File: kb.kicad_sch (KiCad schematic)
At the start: 7 parts, among them J1 USB_C_Receptacle_USB2.0_16P, U1 nRF52840, U2 MIC23051-CGYML

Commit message: more schematics work
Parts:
- added C4: 1u, symbol Device:C
- added C5, C6: 10p, symbol Device:C
- added C7: 0p8, symbol Device:C
- added C8: 0p5, symbol Device:C
- added L2: 4n7, symbol Device:L
- added U3: BQ25185DLHR, Package_SON:WSON-8-1EP_2x2mm_P0.5mm_EP0.9x1.6mm, symbol Battery_Management_Extra:BQ25185DLHR
- added Y1: XRCGB32M000F1S1CR0, symbol Device:Crystal_GND24
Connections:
- net +BATT: no longer C1.1, U2.2 (EN), U2.3 (VSC), U2.7 (VIN)
- net GND: now also U1.B7 (VSS), U1.EP (VSS), U1.F23 (VSS_PA), C4.1, C5.2, C6.2, C7.2, C8.2, U3.5 (GND), U3.9 (STAT1), Y1.2, Y1.4
- net VBUS: now also C4.2, U3.10 (IN)
- net USB_DP: now reaches J1.A6 (D+), J1.B6 (D+)
- net USB_DN: now reaches J1.A7 (D-), J1.B7 (D-)
- net at U1.H23 (ANT): now also C7.1, L2.2
- new net: C1.1, U2.2 (EN), U2.3 (VSC), U2.7 (VIN)
- new net: C8.1, L2.1
- new net XIN: C6.1, Y1.1
- new net XOUT: C5.1, Y1.3
- no-connect marks 3 -> 4
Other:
- note added: "Note: Buy 12p caps for testing"
- moved on the sheet: U1

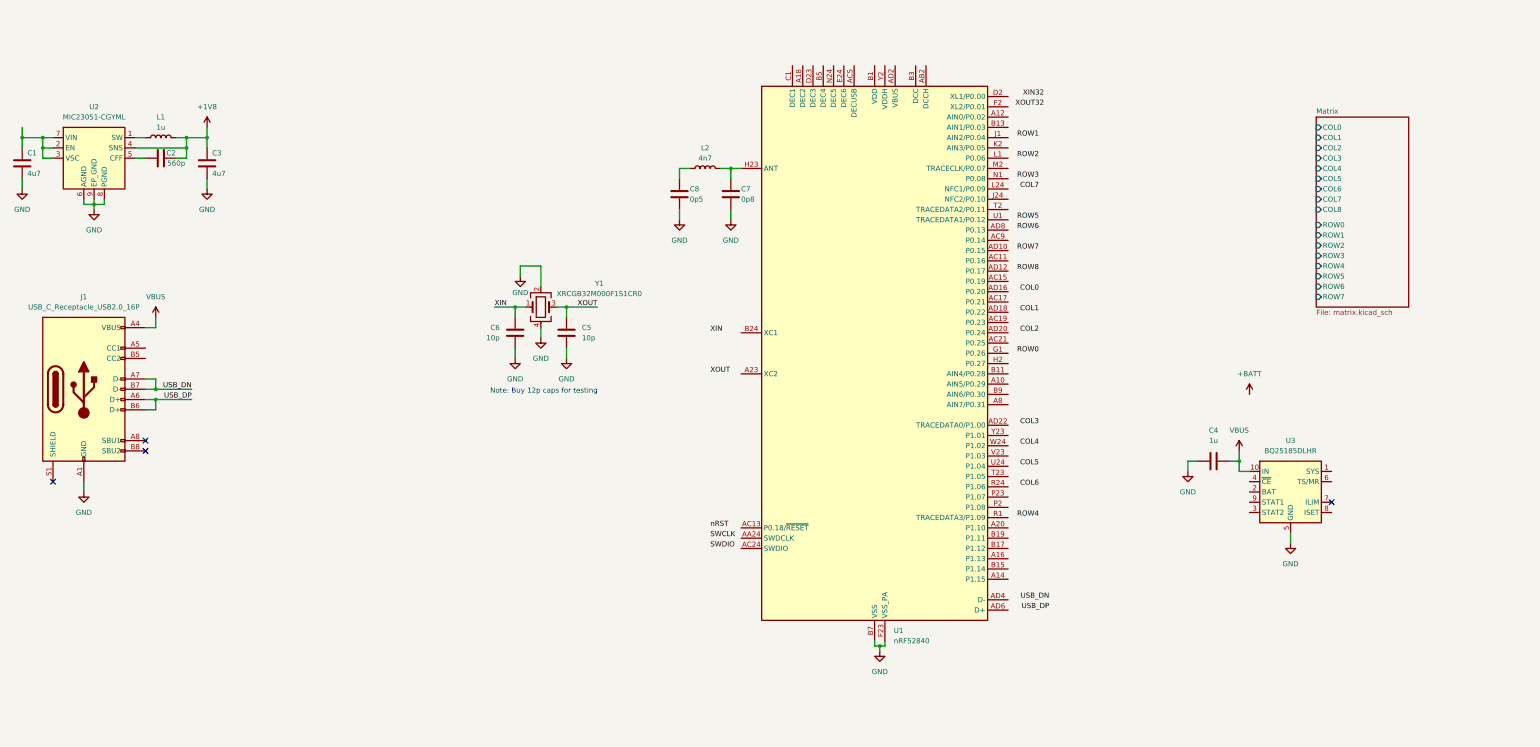
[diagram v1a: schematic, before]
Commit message: update layout and switch to wired
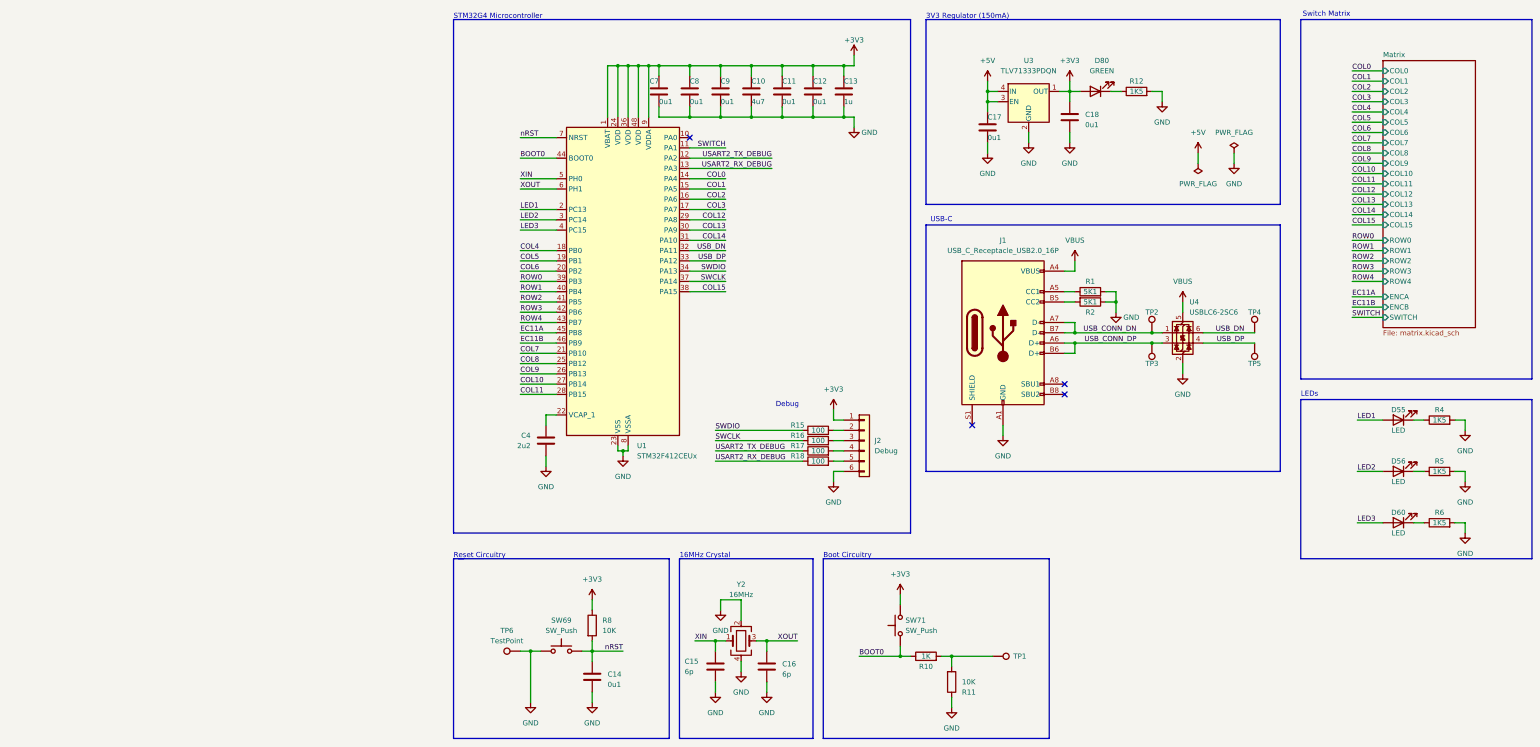
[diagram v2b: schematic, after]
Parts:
- removed C1, C3: 4u7, symbol Device:C
- removed C2: 560p, symbol Device:C
- removed C5, C6: 10p, symbol Device:C
- removed L1: 1u, symbol Device:L
- removed L2: 4n7, symbol Device:L
- removed U1: nRF52840, Package_DFN_QFN:Nordic_AQFN-73-1EP_7x7mm_P0.5mm, symbol MCU_Nordic:nRF52840
- removed U2: MIC23051-CGYML, Package_DFN_QFN:Micrel_MLF-8-1EP_2x2mm_P0.5mm_EP0.6x1.2mm_ThermalVias, symbol Regulator_Switching_Extra:MIC23051-CGYML
- removed U3: BQ25185DLHR, Package_SON:WSON-8-1EP_2x2mm_P0.5mm_EP0.9x1.6mm, symbol Battery_Management_Extra:BQ25185DLHR
- removed Y1: XRCGB32M000F1S1CR0, symbol Device:Crystal_GND24
- added C10: 4u7, Capacitor_SMD:C_0201_0603Metric, symbol Device:C
- added C11, C12, C14, C9: 0u1, Capacitor_SMD:C_0201_0603Metric, symbol Device:C
- added C13: 1u, Capacitor_SMD:C_0201_0603Metric, symbol Device:C
- added C15, C16: 6p, Capacitor_SMD:C_0402_1005Metric, symbol Device:C
- added C17, C18: 0u1, Capacitor_SMD:C_0603_1608Metric, symbol Device:C
- added D55, D56, D60: LED, symbol Device:LED
- added D80: GREEN, LED_SMD:LED_0402_1005Metric, symbol Device:LED
- added J2: Debug, symbol Connector_Generic:Conn_01x06
- added R1, R2: 5K1, symbol Device:R
- added R10: 1K, Resistor_SMD:R_0201_0603Metric, symbol Device:R
- added R11: 10K, Resistor_SMD:R_0402_1005Metric, symbol Device:R
- added R12: 1K5, Resistor_SMD:R_0402_1005Metric, symbol Device:R
- added R15, R16, R17, R18: 100, symbol Device:R
- added R4, R5, R6: 1K5, symbol Device:R
- added R8: 10K, Resistor_SMD:R_0201_0603Metric, symbol Device:R
- added SW69, SW71: SW_Push, symbol Switch:SW_Push
- added TP1: TestPoint, TestPoint:TestPoint_Pad_1.0x1.0mm, symbol Connector:TestPoint
- added TP2, TP3, TP4, TP5, TP6: TestPoint, symbol Connector:TestPoint
- added U1: STM32F412CEUx, Package_DFN_QFN:QFN-48-1EP_7x7mm_P0.5mm_EP5.6x5.6mm, symbol MCU_ST_STM32F4:STM32F412CEUx
- added U3: TLV71333PDQN, Package_SON:Texas_X2SON-4_1x1mm_P0.65mm, symbol TLV71333PDQ:TLV71333PDQN
- added U4: USBLC6-2SC6, Package_TO_SOT_SMD:SOT-23-6, symbol Power_Protection:USBLC6-2SC6
- added Y2: 16MHz, Crystal:Crystal_SMD_2016-4Pin_2.0x1.6mm, symbol Device:Crystal_GND24
- C4: value 1u -> 2u2
- C7: value 0p8 -> 0u1; footprint (none) -> Capacitor_SMD:C_0201_0603Metric; LCSC (none) -> C907967
- C8: value 0p5 -> 0u1; footprint (none) -> Capacitor_SMD:C_0201_0603Metric; LCSC (none) -> C907967
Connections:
- net COL0: now also U1.14 (PA4)
- net COL1: now also U1.15 (PA5)
- net COL2: now also U1.16 (PA6)
- net COL3: now also U1.17 (PA7)
- net COL4: now also U1.18 (PB0)
- net COL5: now also U1.19 (PB1)
- net COL6: now also U1.20 (PB2)
- net COL7: now also U1.21 (PB10)
- net GND: now also C4.2, C10.2, C11.2, C12.2, C13.2, C14.2, C15.2, C16.2, C17.2, C18.2, C9.2, J2.6 (Pin_6), R1.2, R11.1, R12.2, R2.1, R4.2, R5.2, R6.2, SW69.1, TP6.1, U1.23 (VSS), U1.35 (VSS), U1.47 (VSS), U1.49 (VSS), U1.8 (VSSA), U3.2 (GND), U3.5 (GND), U4.2 (GND), Y2.2, Y2.4; no longer C4.1
- net ROW0: now also U1.39 (PB3)
- net ROW1: now also U1.40 (PB4)
- net ROW2: now also U1.41 (PB5)
- net ROW3: now also U1.42 (PB6)
- net ROW4: now also U1.43 (PB7)
- net SWCLK: now also R16.1, U1.37 (PA14)
- net SWDIO: now also R15.1, U1.34 (PA13)
- net USB_DN: now also TP4.1, U1.32 (PA11), U4.6 (I/O1); no longer J1.A7 (D-), J1.B7 (D-)
- net USB_DP: now also TP5.1, U1.33 (PA12), U4.4 (I/O2); no longer J1.A6 (D+), J1.B6 (D+)
- net VBUS: now also U4.5 (VBUS); no longer C4.2
- net XIN: now also C15.1, U1.5 (PH0), Y2.1
- net XOUT: now also C16.1, U1.6 (PH1), Y2.3
- net nRST: now also C14.1, R8.2, SW69.2, U1.7 (NRST)
- net at J1.A5 (CC1): now also R1.1
- net at J1.B5 (CC2): now also R2.2
- net +3V3: now reaches C8.1
- net +3V3: now also C7.1, C10.1, C11.1, C12.1, C13.1, C18.1, C9.1, D80.2 (A), J2.1 (Pin_1), R8.1, SW71.2, U1.1 (VBAT), U1.24 (VDD), U1.36 (VDD), U1.48 (VDD), U1.9 (VDDA), U3.1 (OUT)
- new net: D60.1 (K), R6.1
- new net: D56.1 (K), R5.1
- new net: J2.5 (Pin_5), R18.2
- new net: J2.4 (Pin_4), R17.2
- new net: C4.1, U1.22 (VCAP_1)
- new net: D55.1 (K), R4.1
- new net: R10.2, R11.2, TP1.1
- new net: J2.3 (Pin_3), R16.2
- new net: D80.1 (K), R12.1
- new net: J2.2 (Pin_2), R15.2
- new net +5V: C17.1, U3.3 (EN), U3.4 (IN)
- new net BOOT0: R10.1, SW71.1, U1.44 (BOOT0)
- new net COL10: U1.27 (PB14)
- new net COL11: U1.28 (PB15)
- new net COL12: U1.29 (PA8)
- new net COL13: U1.30 (PA9)
- new net COL14: U1.31 (PA10)
- new net COL15: U1.38 (PA15)
- new net COL8: U1.25 (PB12)
- new net COL9: U1.26 (PB13)
- new net EC11A: U1.45 (PB8)
- new net EC11B: U1.46 (PB9)
- new net LED1: D55.2 (A), U1.2 (PC13)
- new net LED2: D56.2 (A), U1.3 (PC14)
- new net LED3: D60.2 (A), U1.4 (PC15)
- new net SWITCH: U1.11 (PA1)
- new net USART2_RX_DEBUG: R18.1, U1.13 (PA3)
- new net USART2_TX_DEBUG: R17.1, U1.12 (PA2)
- new net USB_CONN_DN: J1.A7 (D-), J1.B7 (D-), TP2.1, U4.1 (I/O1)
- new net USB_CONN_DP: J1.A6 (D+), J1.B6 (D+), TP3.1, U4.3 (I/O2)
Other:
- sheet Matrix ports: added COL10, COL11, COL12, COL13, COL14, COL15, COL9, ENCA, ENCB, SWITCH; removed ROW5, ROW6, ROW7
- note added: "16MHz Crystal"
- note added: "3V3 Regulator (150mA)"
- note added: "Boot Circuitry"
- note added: "Debug"
- note added: "LEDs"
- note added: "Reset Circuitry"
- note added: "STM32G4 Microcontroller"
- note added: "Switch Matrix"
- note added: "USB-C"
- note removed: "Note: Buy 12p caps for testing"
- moved on the sheet: J1

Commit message: work on layout and routing
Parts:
- removed J1: USB_C_Receptacle_USB2.0_16P, symbol Connector:USB_C_Receptacle_USB2.0_16P
- removed R1, R2: 5K1, symbol Device:R
- removed TP2, TP3, TP4, TP5: TestPoint, symbol Connector:TestPoint
- removed U4: USBLC6-2SC6, Package_TO_SOT_SMD:SOT-23-6, symbol Power_Protection:USBLC6-2SC6
- added J2: 78171-0004, Connector_Molex:Molex_Pico-EZmate_78171-0004_1x04-1MP_P1.20mm_Vertical, symbol Connector_Generic_MountingPin:Conn_01x04_MountingPin
- C1: renamed from C7; footprint Capacitor_SMD:C_0201_0603Metric -> Capacitor_SMD:C_0402_1005Metric
- C10: renamed from C4; footprint (none) -> Capacitor_SMD:C_0402_1005Metric
- C13: renamed from C14; footprint Capacitor_SMD:C_0201_0603Metric -> Capacitor_SMD:C_0402_1005Metric
- C2: renamed from C8; footprint Capacitor_SMD:C_0201_0603Metric -> Capacitor_SMD:C_0402_1005Metric
- C3: renamed from C9; footprint Capacitor_SMD:C_0201_0603Metric -> Capacitor_SMD:C_0402_1005Metric
- C4: renamed from C10; footprint Capacitor_SMD:C_0201_0603Metric -> Capacitor_SMD:C_0402_1005Metric
- C5: renamed from C11; footprint Capacitor_SMD:C_0201_0603Metric -> Capacitor_SMD:C_0402_1005Metric
- C6: renamed from C12; footprint Capacitor_SMD:C_0201_0603Metric -> Capacitor_SMD:C_0402_1005Metric
- C7: renamed from C13; footprint Capacitor_SMD:C_0201_0603Metric -> Capacitor_SMD:C_0402_1005Metric
- D100: renamed from D55; footprint (none) -> LED_SMD:LED_0402_1005Metric
- D101: renamed from D56; footprint (none) -> LED_SMD:LED_0402_1005Metric
- D102: renamed from D60; footprint (none) -> LED_SMD:LED_0402_1005Metric
- J1: renamed from J2; footprint (none) -> Connector_PinHeader_2.54mm:PinHeader_1x06_P2.54mm_Vertical
- R10: footprint Resistor_SMD:R_0201_0603Metric -> Resistor_SMD:R_0402_1005Metric
- R2: renamed from R4; footprint (none) -> Resistor_SMD:R_0402_1005Metric
- R3: renamed from R5; footprint (none) -> Resistor_SMD:R_0402_1005Metric
- R4: renamed from R6; footprint (none) -> Resistor_SMD:R_0402_1005Metric
- R5: renamed from R15; footprint (none) -> Resistor_SMD:R_0402_1005Metric
- R6: renamed from R16; footprint (none) -> Resistor_SMD:R_0402_1005Metric
- R7: renamed from R17; footprint (none) -> Resistor_SMD:R_0402_1005Metric
- R8: renamed from R18; footprint (none) -> Resistor_SMD:R_0402_1005Metric
- R9: renamed from R8; footprint Resistor_SMD:R_0201_0603Metric -> Resistor_SMD:R_0402_1005Metric
- TP1: renamed from TP6; footprint (none) -> TestPoint:TestPoint_Pad_1.0x1.0mm
- renumbered C15 to C11, C16 to C12, C18 to C8, C17 to C9, D80 to D103, R12 to R1, SW71 to SW100, SW69 to SW101, TP1 to TP2, U3 to U1, U1 to U2, Y2 to Y1
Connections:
- net +5V: now also J2.1 (Pin_1)
- net GND: now also J2.4 (Pin_4), J2.MP (MountPin)
- net USB_DN: now also J2.2 (Pin_2)
- net USB_DP: now also J2.3 (Pin_3)
- no-connect marks 4 -> 1
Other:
- note added: "USB Daughterboard"
- note removed: "USB-C"
- moved on the sheet: D100, D101, D102, R2, R3, R4

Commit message: backup before encoder fix
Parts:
- removed D101, D102: LED, LED_SMD:LED_0402_1005Metric, symbol Device:LED
- removed R3: 1K5, Resistor_SMD:R_0402_1005Metric, symbol Device:R
- added C17: 0u1, Capacitor_SMD:C_0603_1608Metric, symbol Device:C
- C1, C13, C3, C4, C5, C6, C7: footprint Capacitor_SMD:C_0402_1005Metric -> Capacitor_SMD:C_0603_1608Metric
- C10: footprint Capacitor_SMD:C_0402_1005Metric -> Capacitor_SMD:C_0603_1608Metric; LCSC (none) -> C253012
- Ce: renamed from C2; footprint Capacitor_SMD:C_0402_1005Metric -> Capacitor_SMD:C_0603_1608Metric
- D75: renamed from D100; value LED -> BLUE
- J1: footprint Connector_PinHeader_2.54mm:PinHeader_1x06_P2.54mm_Vertical -> Connector_PinHeader_2.54mm:PinHeader_1x06_P2.54mm_Horizontal
- R1, R11, R2, R5, R6, R7, R9: footprint Resistor_SMD:R_0402_1005Metric -> Resistor_SMD:R_0603_1608Metric
- R10: value 1K -> 10K; footprint Resistor_SMD:R_0402_1005Metric -> Resistor_SMD:R_0603_1608Metric
- R4: value 1K5 -> 10K; footprint Resistor_SMD:R_0402_1005Metric -> Resistor_SMD:R_0603_1608Metric; LCSC (none) -> C102690
- R8: footprint Resistor_SMD:R_0402_1005Metric -> Resistor_SMD:R_0603_1608Metric; LCSC (none) -> C102690
- SW75: renamed from SW100; footprint (none) -> Button_Switch_SMD:SW_SPST_PTS810
- SW76: renamed from SW101; footprint (none) -> Button_Switch_SMD:SW_SPST_PTS810
- U1: footprint Package_SON:Texas_X2SON-4_1x1mm_P0.65mm -> Package_TO_SOT_SMD:SOT-23-5; symbol TLV71333PDQ:TLV71333PDQN -> Regulator_Linear:TLV71333PDBV
- Y1: value 16MHz -> XRCGB16M000FXN20R0
- renumbered D103 to D74
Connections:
- net +3V3: now also U1.5 (OUT); no longer U1.1 (OUT)
- net +5V: now also U1.1 (IN); no longer U1.4 (IN)
- net BOOT0: now also R10.2, C17.1; no longer R10.1, SW75.1
- net COL0: now also U2.38 (PA15); no longer U2.14 (PA4)
- net COL15: now also U2.14 (PA4); no longer U2.38 (PA15)
- net GND: now also C17.2; no longer R4.2, TP1.1, U1.5 (GND)
- net ROW0: now also U2.43 (PB7); no longer U2.39 (PB3)
- net ROW1: now also U2.42 (PB6); no longer U2.40 (PB4)
- net ROW3: now also U2.40 (PB4); no longer U2.42 (PB6)
- net ROW4: now also U2.39 (PB3); no longer U2.43 (PB7)
- net nRST: now also R4.2; no longer R9.2, SW76.2
- net at R4.1: now also R9.2, SW76.2, TP1.1
- net at R11.2, TP2.1: now also R10.1, SW75.1; no longer R10.2
- net LED1 renamed LED
- net LED2: no longer names the net of U2.3 (PC14)
- net LED3: no longer names the net of U2.4 (PC15)
- no-connect marks 1 -> 3
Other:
- note added: "Debug LED"
- note removed: "LEDs"
- moved on the sheet: C1, C10, C13, C3, C4, C5, C6, C7, Ce, D75, J1, R10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

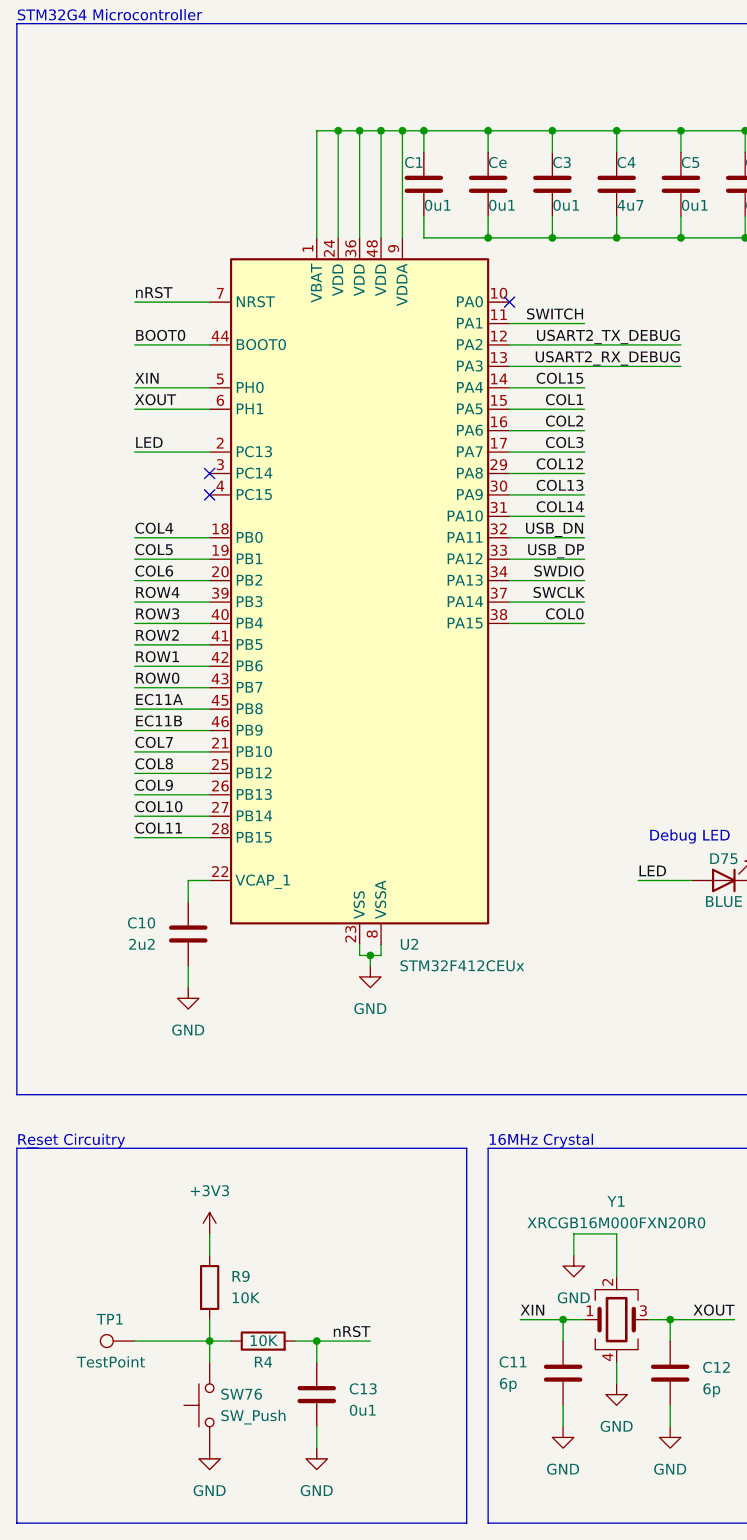
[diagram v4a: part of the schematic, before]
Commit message: fixed encoder
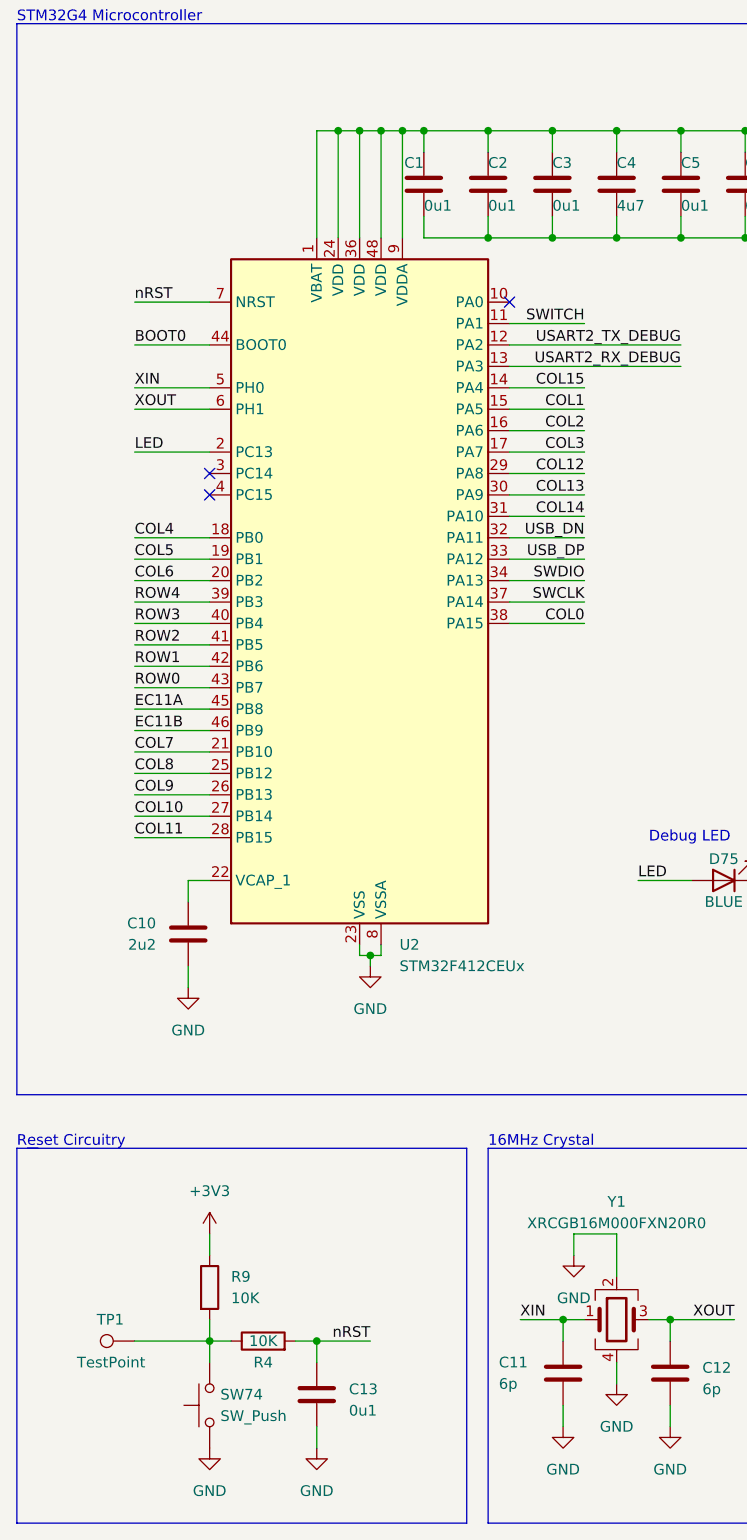
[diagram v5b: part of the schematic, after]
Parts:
- renumbered Ce to C2, SW76 to SW74
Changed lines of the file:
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@@
 		(dnp no)
 		(fields_autoplaced yes)
-		(property "Reference" "SW76"
+		(property "Reference" "SW74"
 			(at 38.1 180.3399 90)
 			(effects
@@
 			(project ""
 				(path "/9cb56eee-d4d8-48bb-94d9-229fa32a5257"
-					(reference "SW76")
+					(reference "SW74")
 					(unit 1)
 				)
@@
 		(on_board yes)
 		(dnp no)
-		(property "Reference" "Ce"
+		(property "Reference" "C2"
 			(at 69.85 34.2899 0)
 			(effects
@@
 			(project "kb"
 				(path "/9cb56eee-d4d8-48bb-94d9-229fa32a5257"
-					(reference "Ce")
-					(unit 1)
-				)
+					(reference "C2")
+					(unit 1)
+				)
